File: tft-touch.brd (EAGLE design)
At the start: 37.5 x 10.9 mm, 2 parts

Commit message: As ordered
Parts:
- added CONN1: STEMMA_I2C_QT, 00jim:JST_SH4
- moved U$1 2.44 mm to (17.9, 9.27), turned to 180 degrees
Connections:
- new net SCL: CONN1.4, JP1.16
- new net SDA: CONN1.3, JP1.14
- net GND: now also CONN1.1
- net S_CS: now also JP1.9; no longer JP1.16
- net T_CS: now also JP1.2; no longer JP1.14
- net VCC: now also CONN1.2
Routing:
- net MISO: track 25.1 -> 51.6 mm, vias 1 -> 0
- net VCC: track 24.2 -> 50.6 mm, vias 1 -> 3
- net T_CS: track 9.20 -> 31.9 mm, vias 0 -> 3
- net SCK: track 15.4 -> 34.5 mm, vias 0 -> 1
- net SDA: track 0.00 -> 18.4 mm, vias 0 -> 3
- net SCL: track 0.00 -> 15.7 mm, vias 0 -> 1
- net S_DC: track 16.8 -> 5.78 mm
- net GND: track 27.6 -> 38.5 mm, vias 0 -> 3
- net S_CS: track 11.8 -> 20.1 mm, vias 0 -> 1
- net MOSI: track 33.1 -> 35.6 mm, vias 0 -> 2
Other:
- board size 37.5 x 10.9 mm -> 36.8 x 11.2 mm

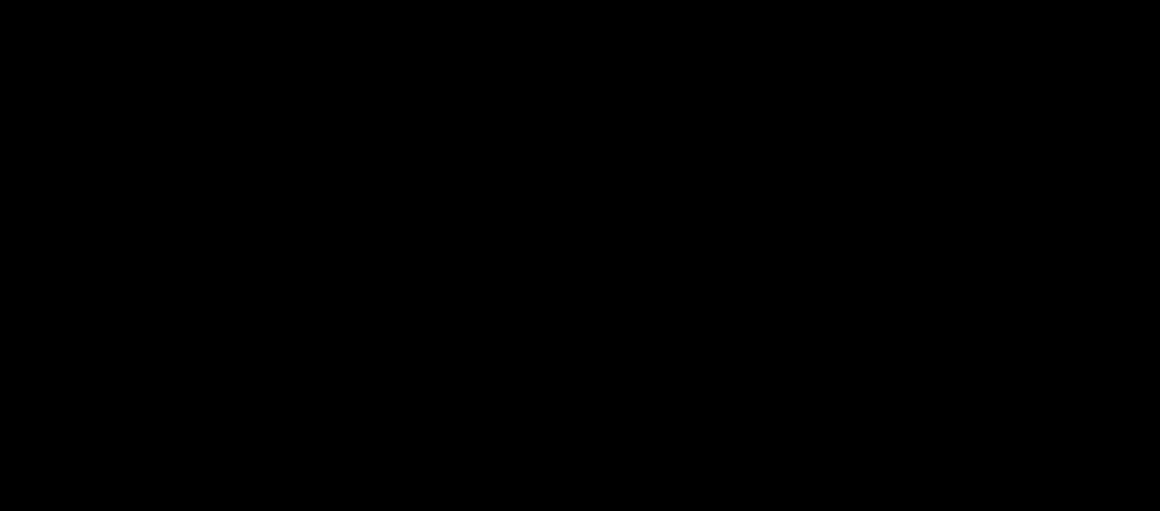
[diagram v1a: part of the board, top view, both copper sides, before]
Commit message: Added more trinkets to TFT touch boards
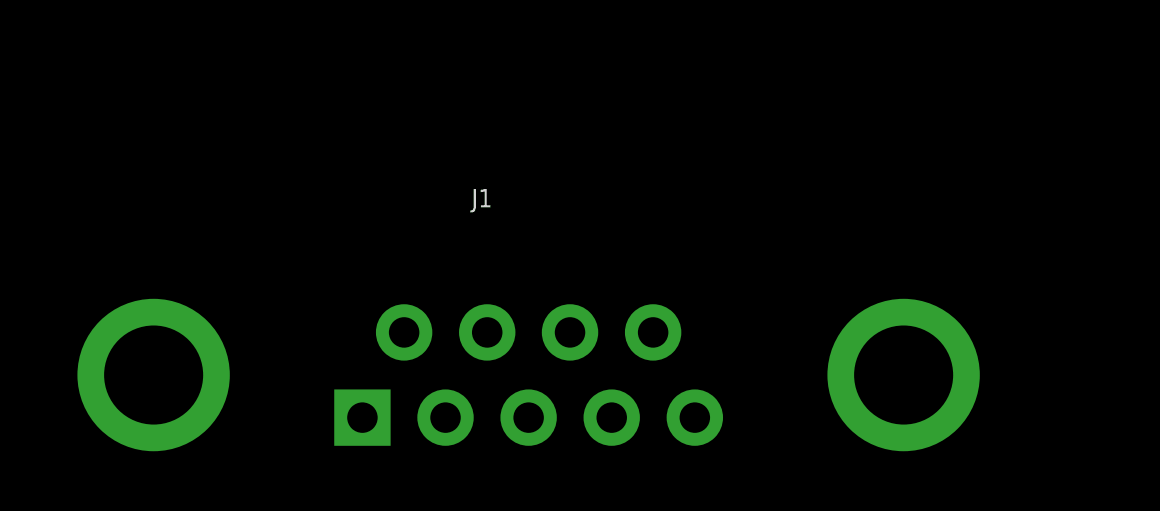
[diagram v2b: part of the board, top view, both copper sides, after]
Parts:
- added J1: (no value), SparkFun-Connectors:DB9
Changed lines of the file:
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@@
 <attribute name="NAME" x="27.531" y="7.17" size="1.778" layer="25"/>
+</element>
+<element name="J1" library="SparkFun-Connectors" package="DB9" value="" x="16.383" y="-16.002" smashed="yes">
+<attribute name="NAME" x="14.478" y="-10.414" size="0.6096" layer="25" font="vector" ratio="20"/>
+<attribute name="PROD_ID" value="CONN-08194" x="16.383" y="-16.002" size="1.778" layer="27" display="off"/>
+<attribute name="VALUE" x="14.478" y="-11.43" size="0.6096" layer="27" font="vector" ratio="20"/>
 </element>
 </elements>

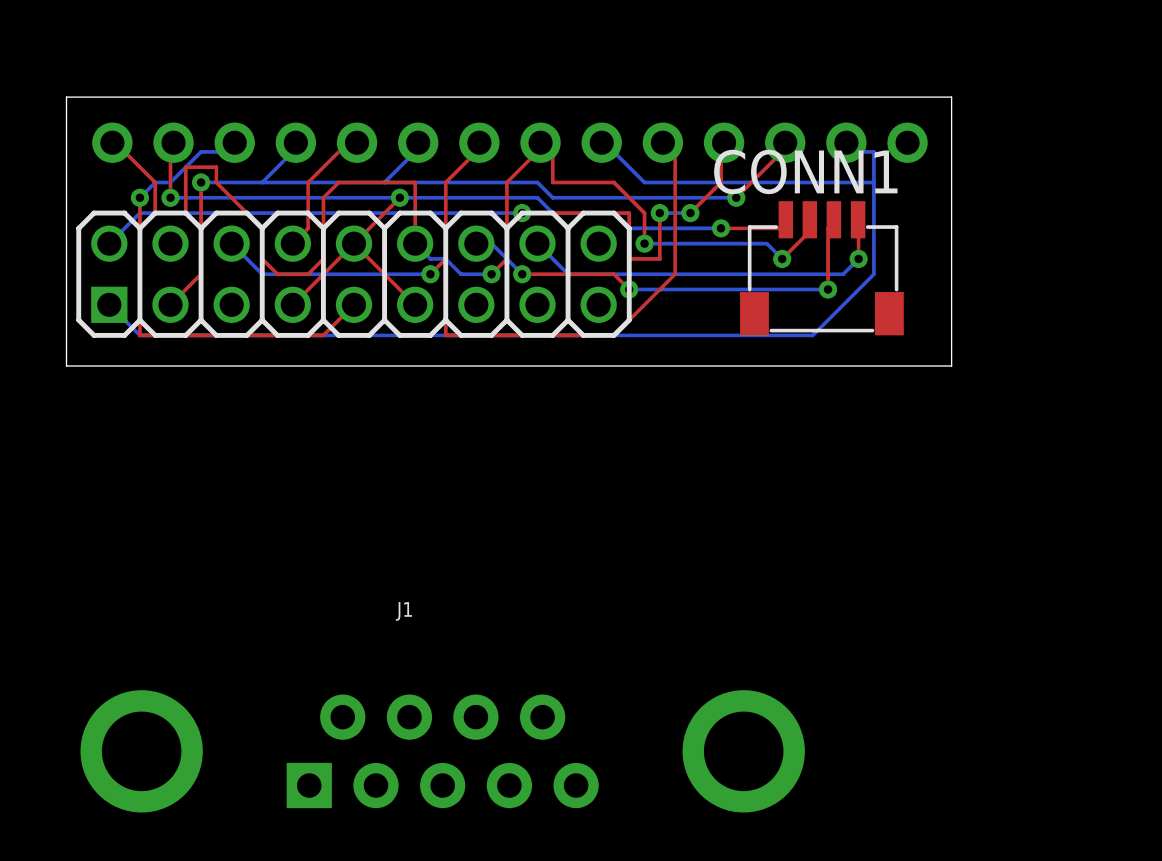
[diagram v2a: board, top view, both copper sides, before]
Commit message: Fix board bug, order again
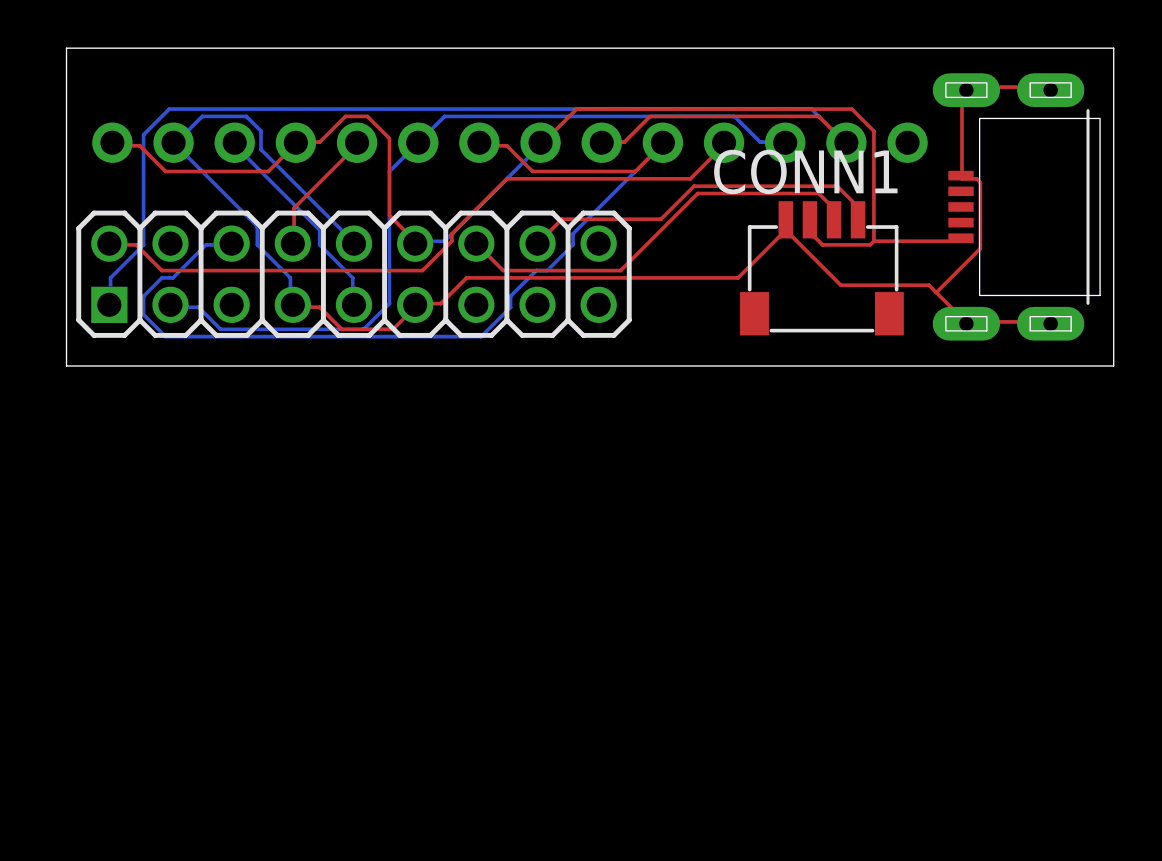
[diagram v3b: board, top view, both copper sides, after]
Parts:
- removed J1: (no value), SparkFun-Connectors:DB9
- added U$2: MICRO-USBV2, microusb:MICRO-USB-2
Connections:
- net GND: now also U$2.5, U$2.P$1, U$2.P$2, U$2.P$3, U$2.P$4
- net MOSI: no longer U$1.11
- net VCC: now also U$1.11, U$2.1
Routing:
- net GND: track 38.5 -> 69.3 mm, vias 3 -> 0
- net S_CS: track 20.1 -> 8.77 mm, vias 1 -> 0
- net SCK: track 34.5 -> 39.8 mm, vias 1 -> 0
- net T_CS: track 31.9 -> 28.4 mm, vias 3 -> 0
- net MISO: track 51.6 -> 48.9 mm
- net MOSI: track 35.6 -> 33.3 mm, vias 2 -> 0
- net VCC: track 50.6 -> 51.7 mm, vias 3 -> 0
- net SDA: track 18.4 -> 17.4 mm, vias 3 -> 0
- net SCL: track 15.7 -> 15.2 mm, vias 1 -> 0
- net S_DC: track 5.78 -> 5.28 mm
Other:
- board size 36.8 x 11.2 mm -> 43.5 x 13.2 mm

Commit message: Enlarged usb pin holes
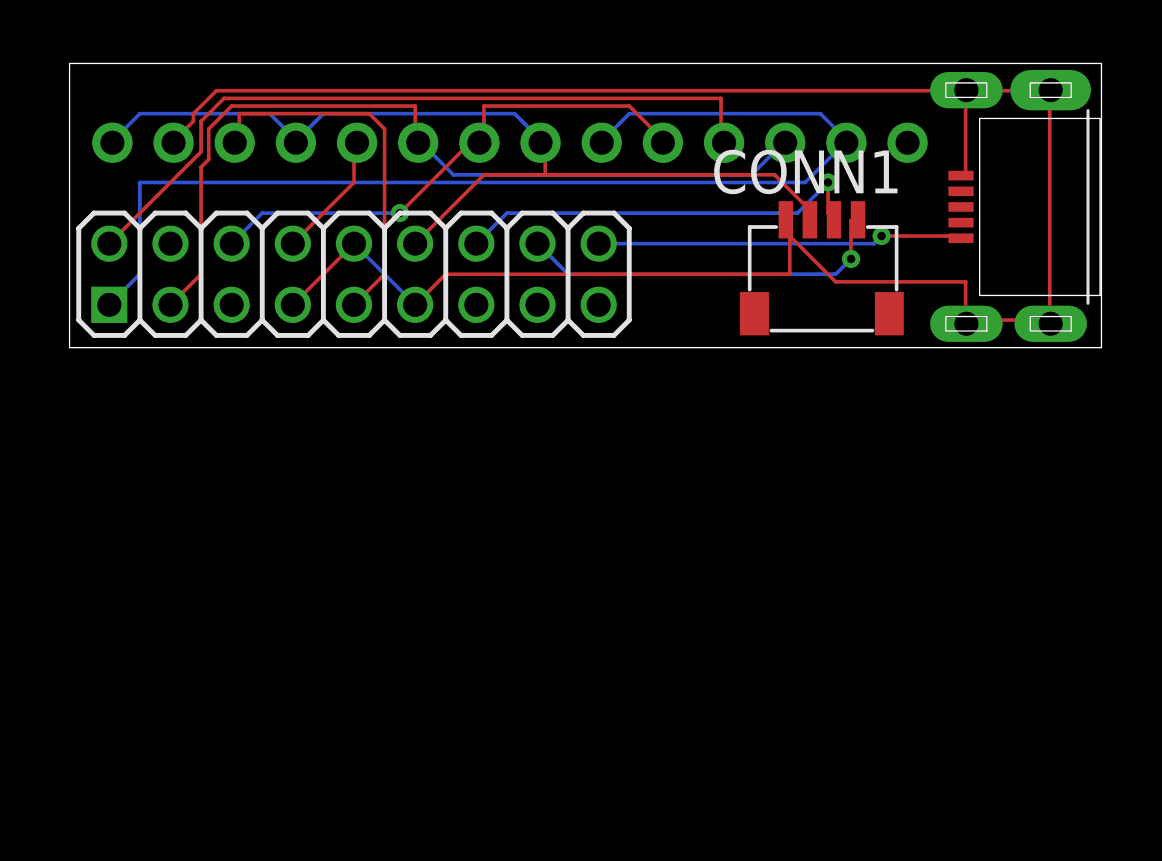
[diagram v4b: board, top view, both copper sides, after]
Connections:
- removed net V50: JP1.18
- new net VCC_50: JP1.18, U$2.1
- net VCC: no longer U$2.1
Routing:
- net GND: track 69.3 -> 90.6 mm
- net SCK: track 39.8 -> 22.0 mm, vias 0 -> 1
- net VCC_50: track 0.00 -> 15.2 mm, vias 0 -> 1
- net VCC: track 51.7 -> 40.0 mm
- net S_CS: track 8.77 -> 15.4 mm
- net T_CS: track 28.4 -> 30.5 mm
- net MISO: track 48.9 -> 46.8 mm
- net MOSI: track 33.3 -> 34.8 mm
- net SCL: track 15.2 -> 15.7 mm, vias 0 -> 1
- net SDA: track 17.4 -> 17.3 mm, vias 0 -> 1
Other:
- board size 43.5 x 13.2 mm -> 42.8 x 11.8 mm

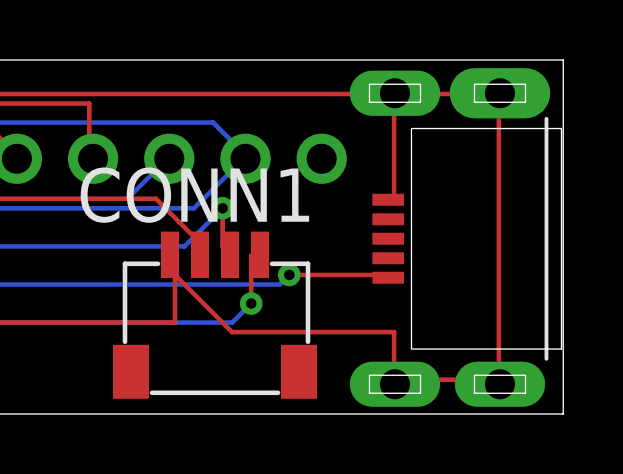
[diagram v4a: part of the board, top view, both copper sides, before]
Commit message: Fix USB connector dimensions
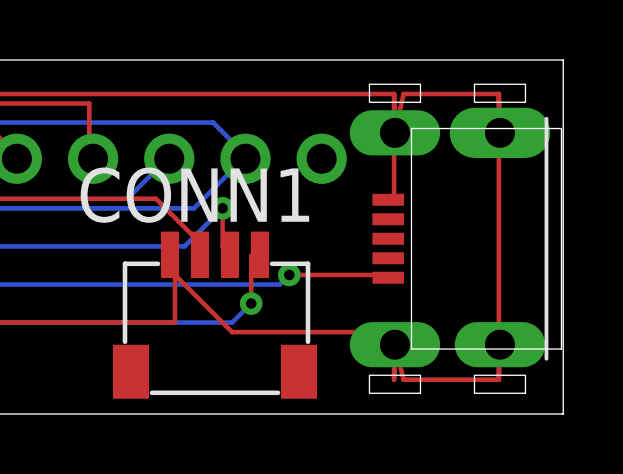
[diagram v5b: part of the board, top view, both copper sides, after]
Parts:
- U$2: device microusb:MICRO-USB-2 -> 01jim:MICRO-USB-2
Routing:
- net GND: track 90.6 -> 97.1 mm
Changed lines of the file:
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@@
 <attribute name="NAME" x="27.531" y="7.17" size="1.778" layer="25"/>
 </element>
-<element name="U$2" library="microusb" package="MICRO-USB-2" value="MICRO-USBV2" x="43.18" y="6.604" smashed="yes" rot="R90"/>
+<element name="U$2" library="01jim" package="MICRO-USB-2" value="MICRO-USBV2" x="43.18" y="6.604" smashed="yes" rot="R90"/>
 </elements>
 <signals>
@@
 <wire x1="38.1" y1="1.905" x2="38.1" y2="3.4925" width="0.1524" layer="1"/>
 <wire x1="30.7975" y1="6.0325" x2="30.631" y2="6.07" width="0.1524" layer="1"/>
-<wire x1="38.1" y1="1.905" x2="38.13" y2="1.754" width="0.1524" layer="1"/>
+<wire x1="38.1" y1="1.905" x2="38.13" y2="3.0734" width="0.1524" layer="1"/>
 <wire x1="38.4175" y1="1.905" x2="41.5925" y2="1.905" width="0.1524" layer="1"/>
-<wire x1="38.4175" y1="1.905" x2="38.13" y2="1.754" width="0.1524" layer="1"/>
+<wire x1="38.4175" y1="1.905" x2="38.13" y2="3.0734" width="0.1524" layer="1"/>
 <wire x1="16.51" y1="3.81" x2="15.24" y2="2.54" width="0.1524" layer="1"/>
 <wire x1="30.7975" y1="3.81" x2="16.51" y2="3.81" width="0.1524" layer="1"/>
@@
 <wire x1="38.1" y1="11.43" x2="6.985" y2="11.43" width="0.1524" layer="1"/>
 <wire x1="5.3975" y1="9.525" x2="5.207" y2="9.271" width="0.1524" layer="1"/>
-<wire x1="38.1" y1="11.43" x2="38.13" y2="11.454" width="0.1524" layer="1"/>
+<wire x1="38.1" y1="11.43" x2="38.13" y2="10.1346" width="0.1524" layer="1"/>
 <wire x1="38.4175" y1="11.43" x2="41.5925" y2="11.43" width="0.1524" layer="1"/>
-<wire x1="38.4175" y1="11.43" x2="38.13" y2="11.454" width="0.1524" layer="1"/>
+<wire x1="38.4175" y1="11.43" x2="38.13" y2="10.1346" width="0.1524" layer="1"/>
 <wire x1="41.5925" y1="11.43" x2="41.5925" y2="1.905" width="0.1524" layer="1"/>
-<wire x1="41.5925" y1="1.905" x2="41.63" y2="1.754" width="0.1524" layer="1"/>
-<wire x1="41.5925" y1="11.43" x2="41.63" y2="11.454" width="0.1524" layer="1"/>
+<wire x1="41.5925" y1="1.905" x2="41.63" y2="3.0734" width="0.1524" layer="1"/>
+<wire x1="41.5925" y1="11.43" x2="41.63" y2="10.1346" width="0.1524" layer="1"/>
 </signal>
 <signal name="VCC">
